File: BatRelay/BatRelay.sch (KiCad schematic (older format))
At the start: 9 parts

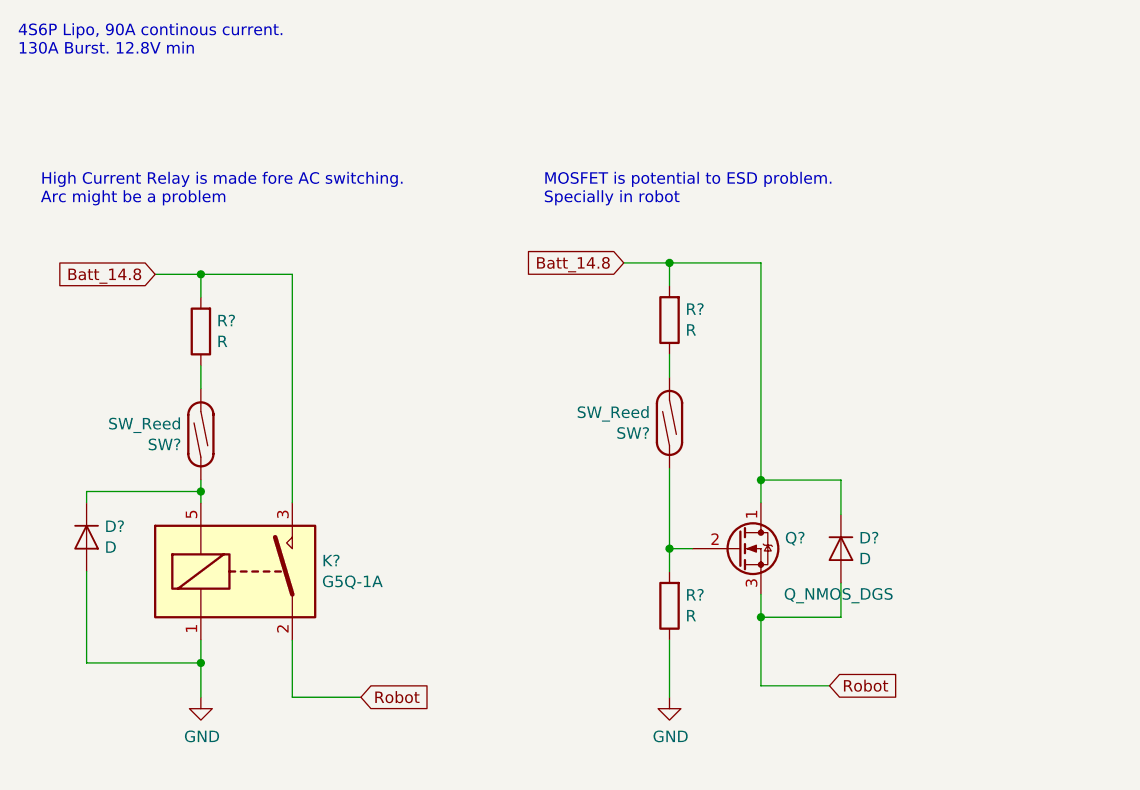
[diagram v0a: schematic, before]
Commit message: added ESD zener for MOSFET design
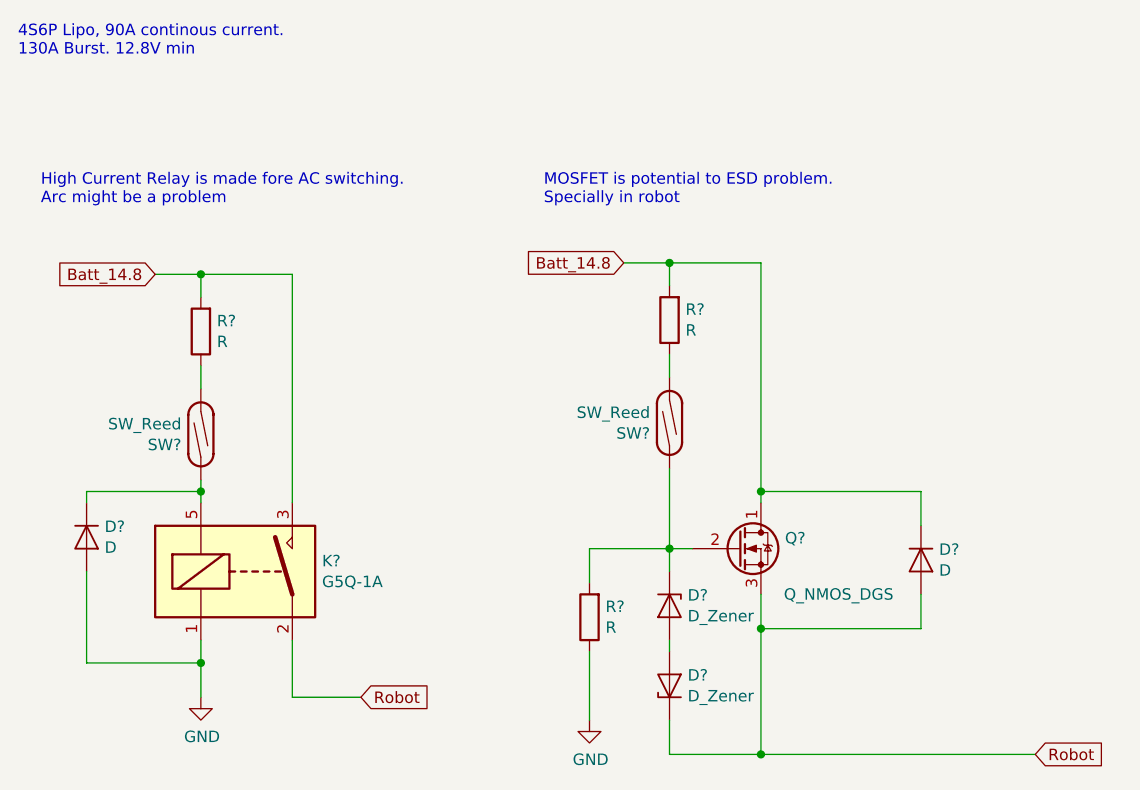
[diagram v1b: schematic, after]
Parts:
- added D? (x2): D_Zener, symbol Device:D_Zener
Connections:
- net Robot: now also D?.1 (K)
- net at Q?.2 (G), R?.2, SW?.1: now also D?.1 (K)
- new net: D?.2 (A), D?.2 (A)
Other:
- moved on the sheet: D?, R?
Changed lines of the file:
@@
 L power:GND #PWR?
 U 1 1 5DC3DBDD
-P 4000 3700
-F 0 "#PWR?" H 4000 3450 50  0001 C CNN
-F 1 "GND" H 4005 3527 50  0000 C CNN
-F 2 "" H 4000 3700 50  0001 C CNN
-F 3 "" H 4000 3700 50  0001 C CNN
-	1    4000 3700
+P 3650 3800
+F 0 "#PWR?" H 3650 3550 50  0001 C CNN
+F 1 "GND" H 3655 3627 50  0000 C CNN
+F 2 "" H 3650 3800 50  0001 C CNN
+F 3 "" H 3650 3800 50  0001 C CNN
+	1    3650 3800
 	1    0    0    -1
 $EndComp
-Text GLabel 4700 3650 2    50   Input ~ 0
+Text GLabel 5600 3950 2    50   Input ~ 0
 Robot
-Wire Wire Line
-	4400 3650 4700 3650
 Wire Wire Line
 	3800 1800 4000 1800
@@
 L Device:D D?
 U 1 1 5DC3DBEE
-P 4750 3050
-F 0 "D?" V 4704 3129 50  0000 L CNN
-F 1 "D" V 4795 3129 50  0000 L CNN
-F 2 "" H 4750 3050 50  0001 C CNN
-F 3 "~" H 4750 3050 50  0001 C CNN
-	1    4750 3050
+P 5100 3100
+F 0 "D?" V 5054 3179 50  0000 L CNN
+F 1 "D" V 5145 3179 50  0000 L CNN
+F 2 "" H 5100 3100 50  0001 C CNN
+F 3 "~" H 5100 3100 50  0001 C CNN
+	1    5100 3100
 	0    1    1    0
 $EndComp
@@
 $EndComp
 Wire Wire Line
-	4400 1800 4400 2750
-Wire Wire Line
-	4400 3250 4400 3350
-Wire Wire Line
 	4000 3050 4100 3050
 Wire Wire Line
-	4750 2900 4750 2750
-Wire Wire Line
-	4750 2750 4400 2750
-Connection ~ 4400 2750
-Wire Wire Line
-	4400 2750 4400 2850
-Wire Wire Line
-	4750 3200 4750 3350
-Wire Wire Line
-	4750 3350 4400 3350
-Connection ~ 4400 3350
-Wire Wire Line
-	4400 3350 4400 3650
-Wire Wire Line
 	4000 2700 4000 3050
-Wire Wire Line
-	4000 3450 4000 3700
 $Comp
 L Device:R R?
 U 1 1 5DC3FB09
-P 4000 3300
-F 0 "R?" H 3930 3254 50  0000 R CNN
-F 1 "R" H 3930 3345 50  0000 R CNN
-F 2 "" V 3930 3300 50  0001 C CNN
-F 3 "~" H 4000 3300 50  0001 C CNN
-	1    4000 3300
+P 3650 3350
+F 0 "R?" H 3580 3304 50  0000 R CNN
+F 1 "R" H 3580 3395 50  0000 R CNN
+F 2 "" V 3580 3350 50  0001 C CNN
+F 3 "~" H 3650 3350 50  0001 C CNN
+	1    3650 3350
 	-1   0    0    1
 $EndComp
-Wire Wire Line
-	4000 3050 4000 3150
 Connection ~ 4000 3050
 Text Notes 1250 1550 0    50   ~ 0
@@
 Text Notes 3450 1550 0    50   ~ 0
 MOSFET is potential to ESD problem. \nSpecially in robot
+$Comp
+L Device:D_Zener D?
+U 1 1 5DC40F21
+P 4000 3300
+F 0 "D?" V 3954 3379 50  0000 L CNN
+F 1 "D_Zener" V 4045 3379 50  0000 L CNN
+F 2 "" H 4000 3300 50  0001 C CNN
+F 3 "~" H 4000 3300 50  0001 C CNN
+	1    4000 3300
+	0    1    1    0
+$EndComp
+$Comp
+L Device:D_Zener D?
+U 1 1 5DC417FD
+P 4000 3650
+F 0 "D?" V 4046 3571 50  0000 R CNN
+F 1 "D_Zener" V 3955 3571 50  0000 R CNN
+F 2 "" H 4000 3650 50  0001 C CNN
+F 3 "~" H 4000 3650 50  0001 C CNN
+	1    4000 3650
+	0    -1   -1   0
+$EndComp
+Wire Wire Line
+	4400 3250 4400 3400
+Wire Wire Line
+	4400 1800 4400 2800
+Wire Wire Line
+	4400 3950 5600 3950
+Wire Wire Line
+	4000 3050 4000 3150
+Wire Wire Line
+	4000 3450 4000 3500
+Wire Wire Line
+	4000 3800 4000 3950
+Wire Wire Line
+	4000 3950 4400 3950
+Connection ~ 4400 3950
+Wire Wire Line
+	4400 2800 5100 2800
+Wire Wire Line
+	5100 2800 5100 2950
+Connection ~ 4400 2800
+Wire Wire Line
+	4400 2800 4400 2850
+Wire Wire Line
+	5100 3250 5100 3400
+Wire Wire Line
+	5100 3400 4400 3400
+Connection ~ 4400 3400
+Wire Wire Line
+	4400 3400 4400 3950
+Wire Wire Line
+	4000 3050 3650 3050
+Wire Wire Line
+	3650 3050 3650 3200
+Wire Wire Line
+	3650 3500 3650 3800
 $EndSCHEMATC
